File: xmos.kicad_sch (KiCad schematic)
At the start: 11 parts, among them U1 XU316-1024-QF60B-C32, Y1 24M

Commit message: Incremental Progress
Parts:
- added FB1: FerriteBead, symbol Device:FerriteBead
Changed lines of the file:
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@@
+	)
+	(symbol
+		(lib_id "Device:FerriteBead")
+		(at 121.92 55.88 90)
+		(unit 1)
+		(exclude_from_sim no)
+		(in_bom yes)
+		(on_board yes)
+		(dnp no)
+		(property "Reference" "FB1"
+			(at 121.8692 63.5 90)
+			(effects
+				(font
+					(size 1.27 1.27)
+				)
+			)
+		)
+		(property "Value" "FerriteBead"
+			(at 121.8692 60.96 90)
+			(effects
+				(font
+					(size 1.27 1.27)
+				)
+			)
+		)
+		(property "Footprint" ""
+			(at 121.92 57.658 90)
+			(effects
+				(font
+					(size 1.27 1.27)
+				)
+				(hide yes)
+			)
+		)
+		(property "Datasheet" "~"
+			(at 121.92 55.88 0)
+			(effects
+				(font
+					(size 1.27 1.27)
+				)
+				(hide yes)
+			)
+		)
+		(property "Description" "Ferrite bead"
+			(at 121.92 55.88 0)
+			(effects
+				(font
+					(size 1.27 1.27)
+				)
+				(hide yes)
+			)
+		)
+		(pin "1"
+		)
+		(pin "2"
+		)
+		(instances
+			(project ""
+				(path "/b16dfd04-6bfc-4d2d-ba2c-9a843d57dfb1/9717bff4-43fd-4c4d-9ccb-a8f356b7f1f3"
+					(reference "FB1")
+					(unit 1)
+				)
+			)
+		)
 	)
 	(symbol

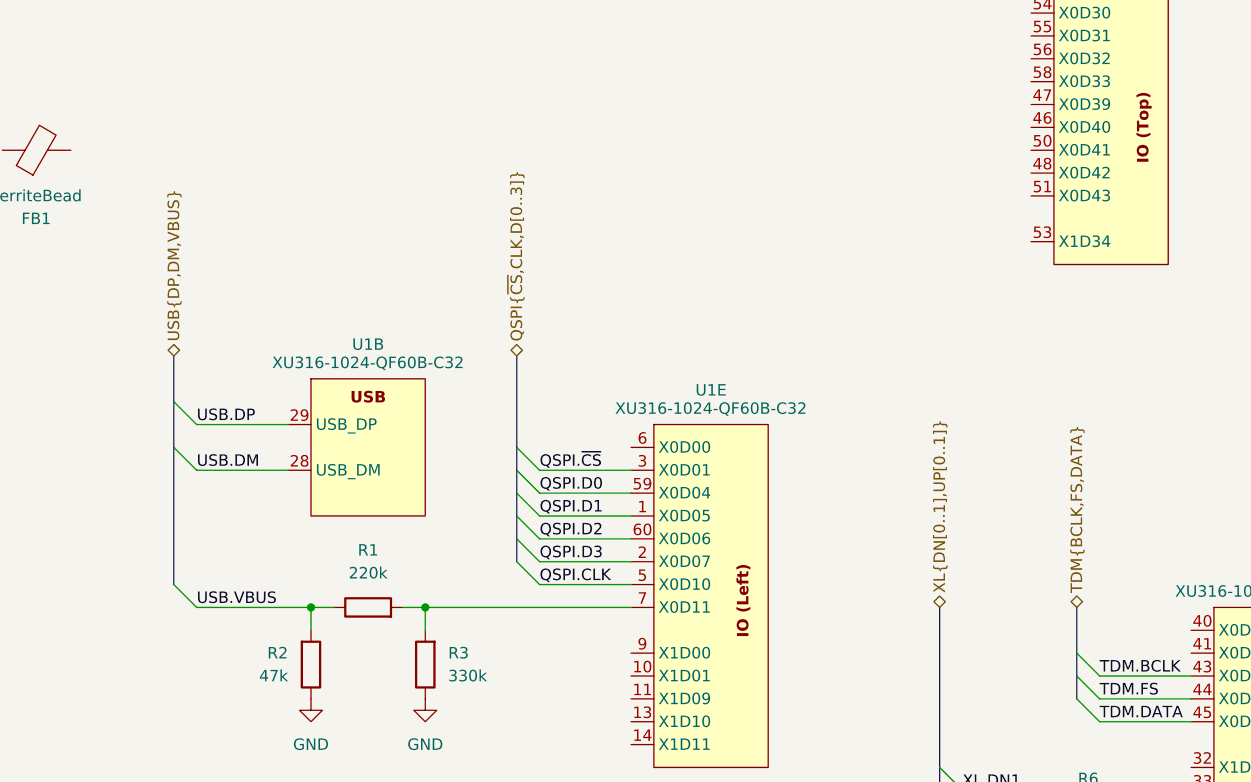
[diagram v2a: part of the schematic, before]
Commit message: Converted connector power to global labels
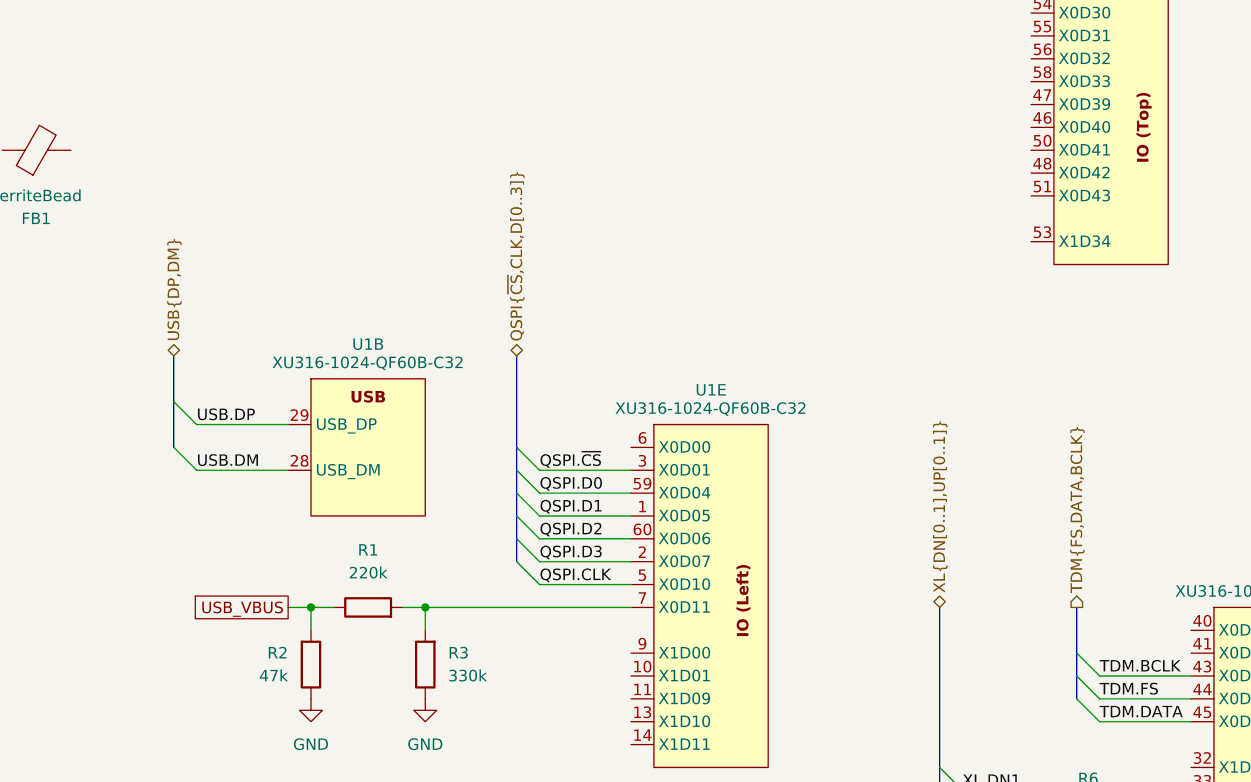
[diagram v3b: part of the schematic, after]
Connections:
- net USB.VBUS renamed USB_VBUS

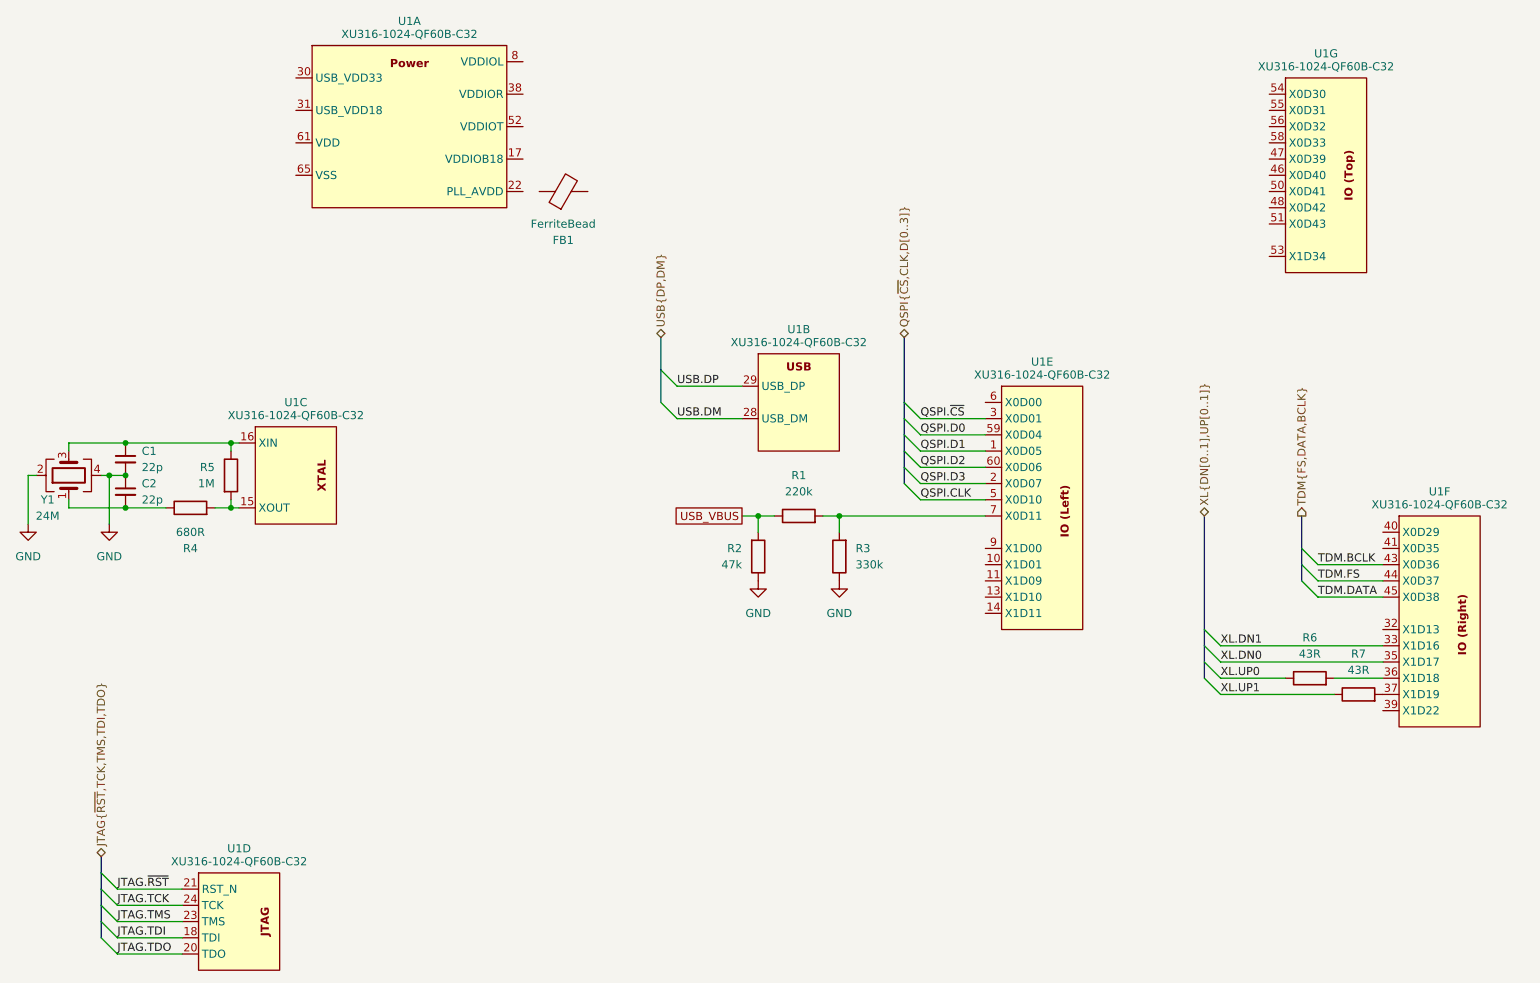
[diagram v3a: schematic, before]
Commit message: Added pMCU
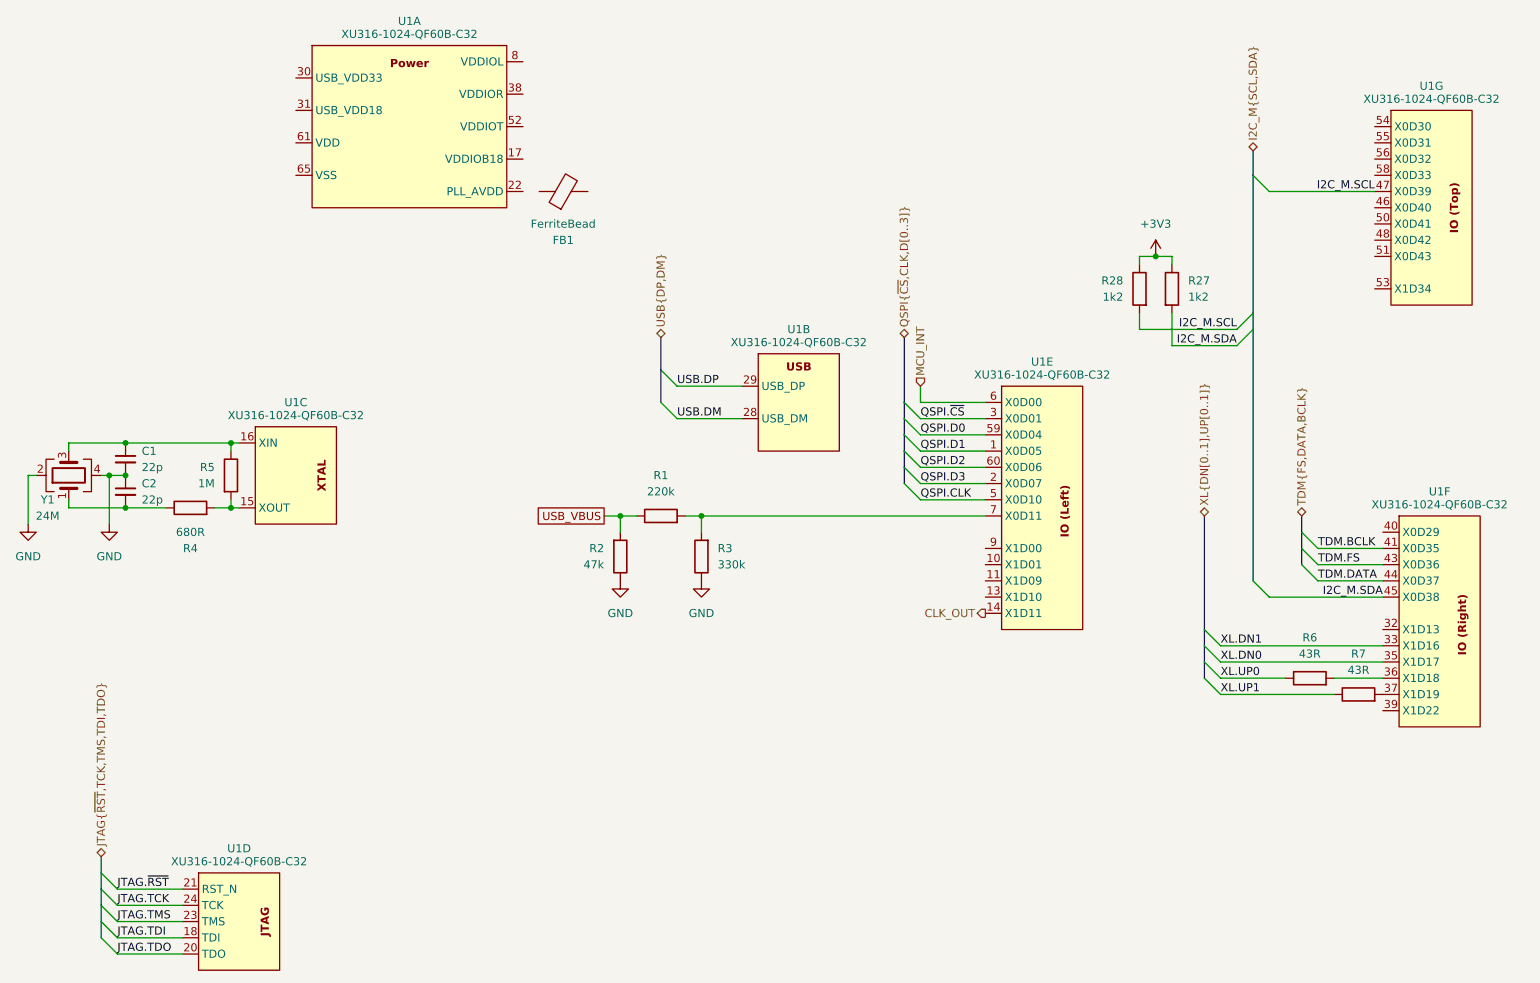
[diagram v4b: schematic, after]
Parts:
- added R27, R28: 1k2, symbol Device:R
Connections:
- net TDM.BCLK: now also U1.41 (X0D35); no longer U1.43 (X0D36)
- net TDM.DATA: now also U1.44 (X0D37); no longer U1.45 (X0D38)
- net TDM.FS: now also U1.43 (X0D36); no longer U1.44 (X0D37)
- net I2C_M.SCL: now reaches U1.47 (X0D39)
- net I2C_M.SCL: now also R28.2
- net CLK_OUT: now reaches U1.14 (X1D11)
- net MCU_INT: now reaches U1.6 (X0D00)
- new net +3V3: R27.1, R28.1
- new net I2C_M.SDA: R27.2, U1.45 (X0D38)
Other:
- moved on the sheet: R1, R2, R3, U1G
